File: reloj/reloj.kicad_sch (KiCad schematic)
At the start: 15 parts, among them J1 Barrel_Jack, J2 Barrel_Jack, J3 Conn_01x02, U1 NE555P

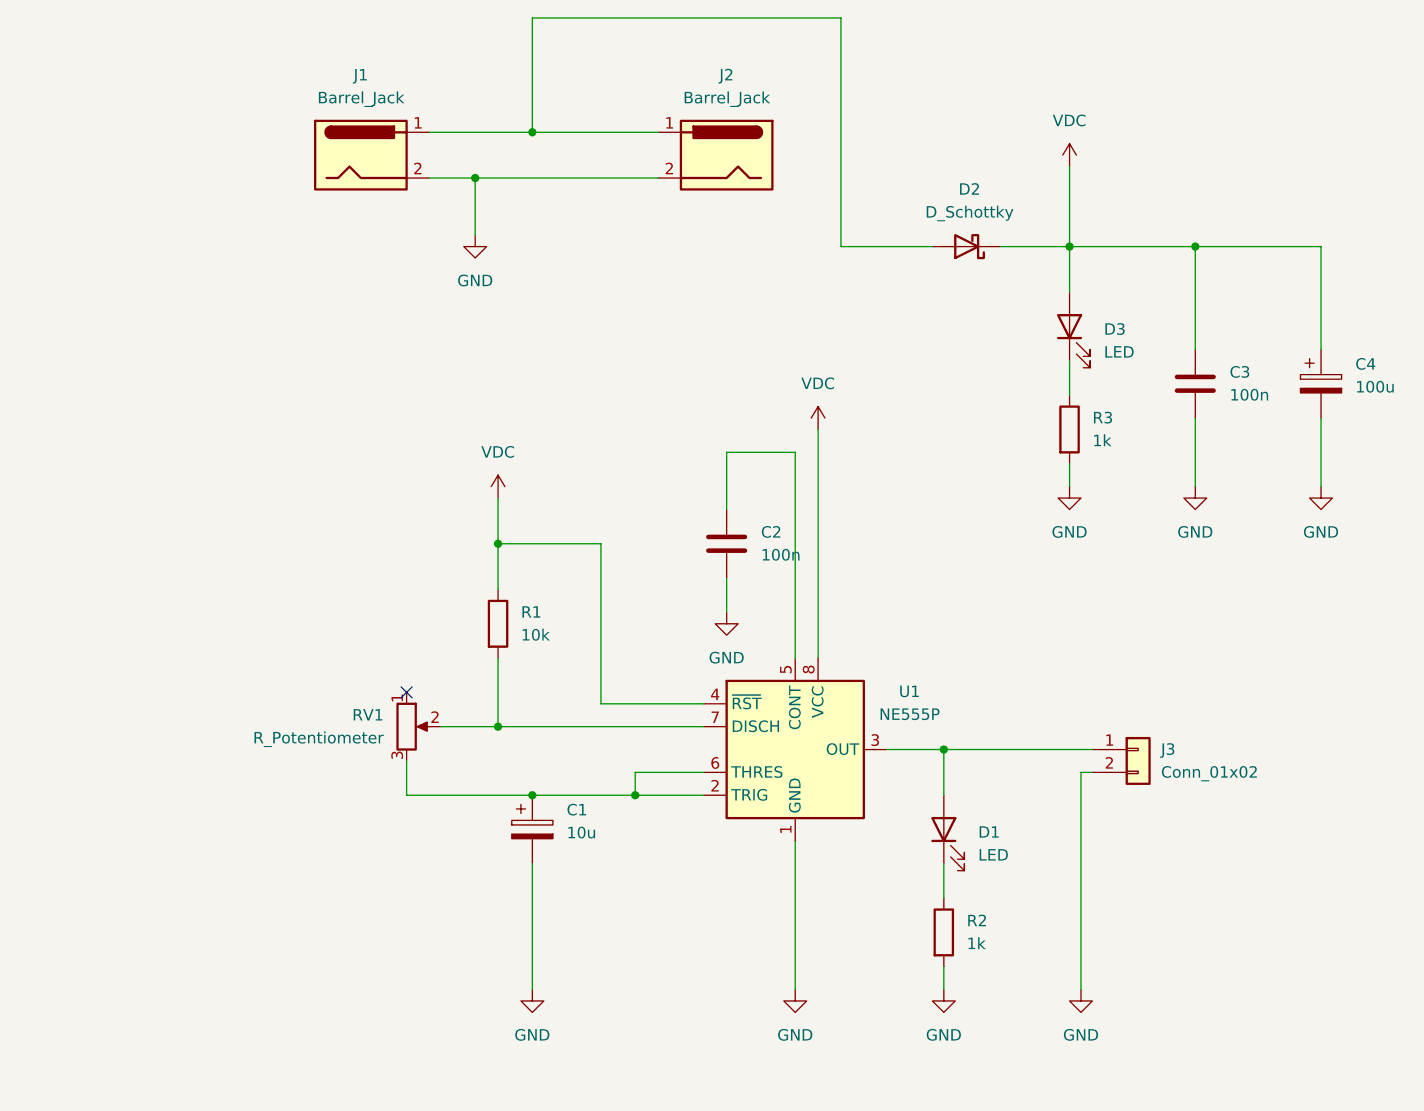
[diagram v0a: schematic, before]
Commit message: convertir de a4 a a5
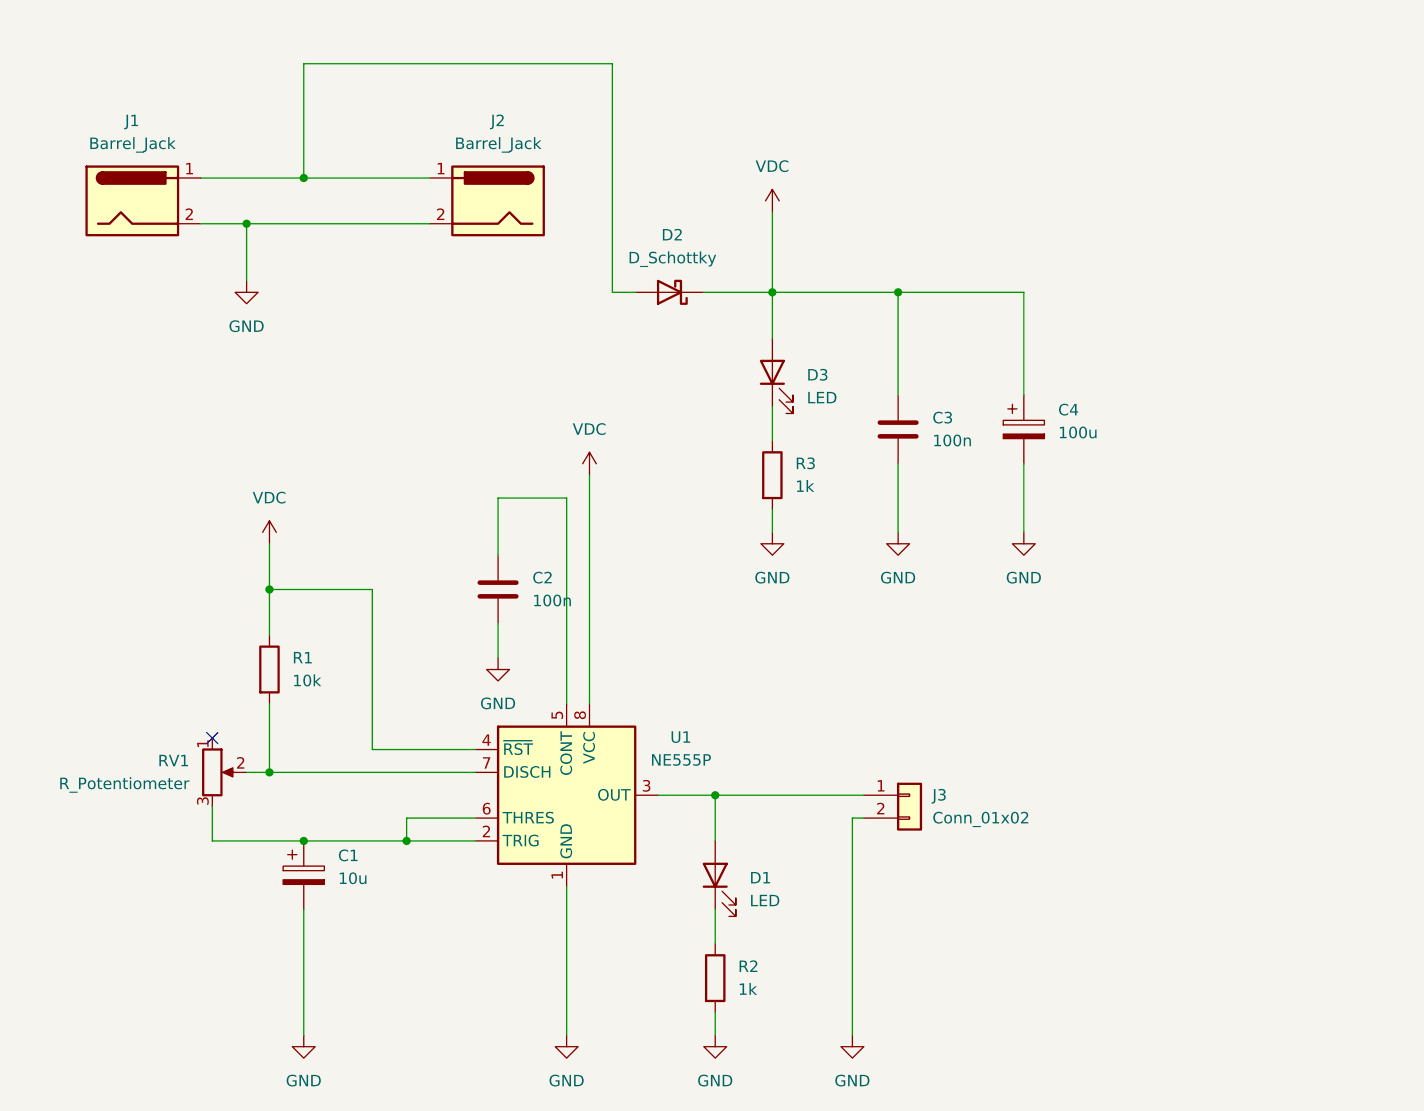
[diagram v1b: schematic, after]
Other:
- moved on the sheet: C1, C2, C3, C4, D1, D2, D3, J1, J2, J3, R1, R2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
